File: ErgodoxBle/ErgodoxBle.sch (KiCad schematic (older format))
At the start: 93 parts, among them SW0:10 SW0:3, SW0:11 SW0:2, SW0:12 SW0:1, SW0:7 SW0:6, SW0:8 SW0:5, SW0:9 SW0:4, SW1:10 SW1:3, SW1:11 SW1:2, SW1:12 SW1:1, SW1:13 SW1:0, SW1:9 SW1:4, SW2:10 SW2:3, SW2:11 SW2:2, SW2:12 SW2:1, SW2:13 SW2:0, SW2:7 SW2:6, SW2:8 SW2:5, SW2:9 SW2:4, SW3:10 SW3:3, SW3:11 SW3:2, SW3:12 SW3:1, SW3:13 SW3:0, SW3:8 SW3:5, SW3:9 SW3:4, SW4:10 SW4:3, SW4:11 SW4:2, SW4:12 SW4:1, SW4:13 SW4:0, SW4:7 SW4:6, SW4:8 SW4:5, SW4:9 SW4:4, SW5:10 SW5:3, SW5:11 SW5:2, SW5:12 SW5:1, SW5:13 SW5:0, SW5:7 SW5:6, SW5:8 SW5:5, SW5:9 SW5:4

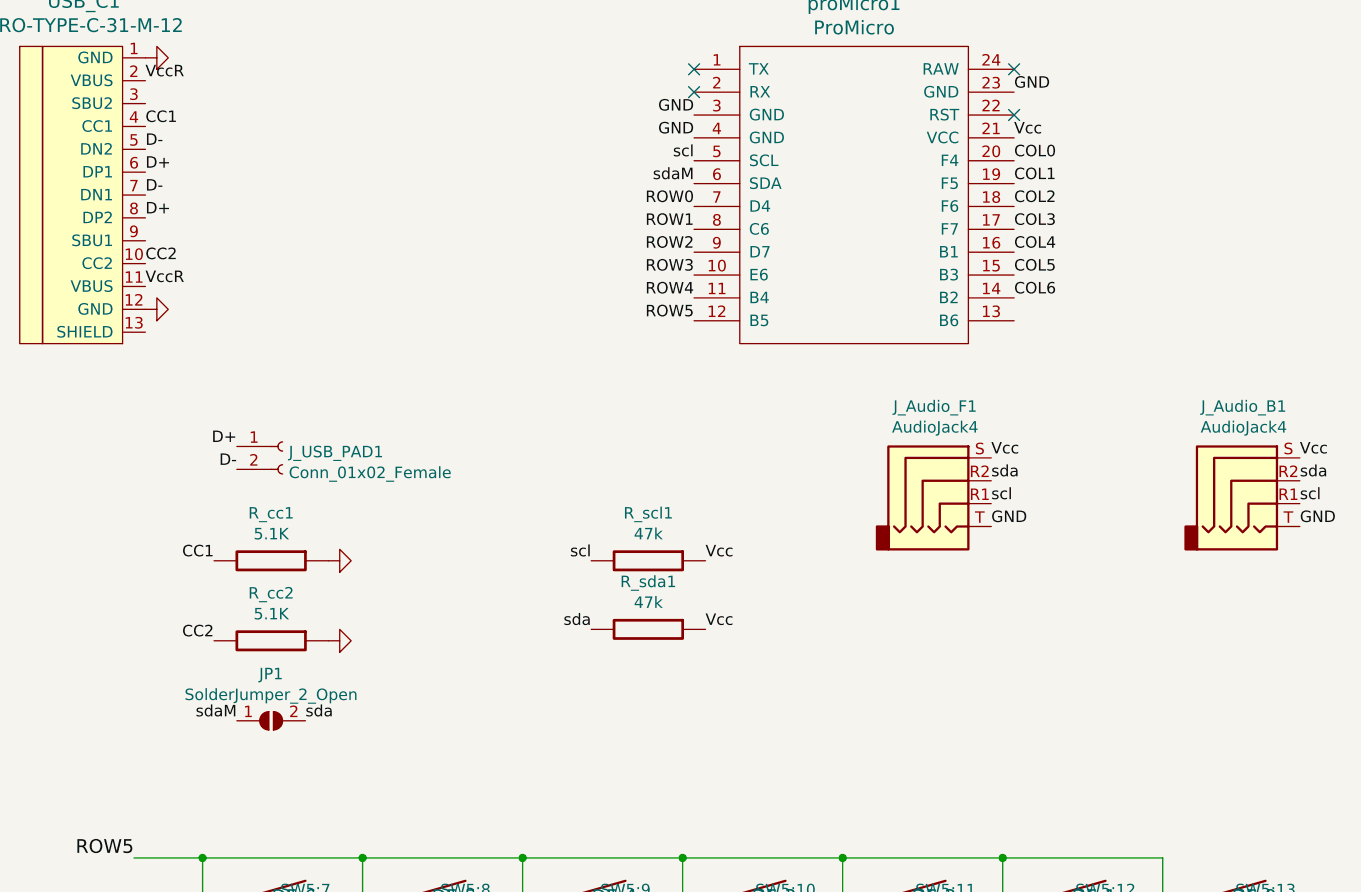
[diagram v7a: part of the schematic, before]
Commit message: update pcb, removed unwanted i2c wire, will go only serial over sda
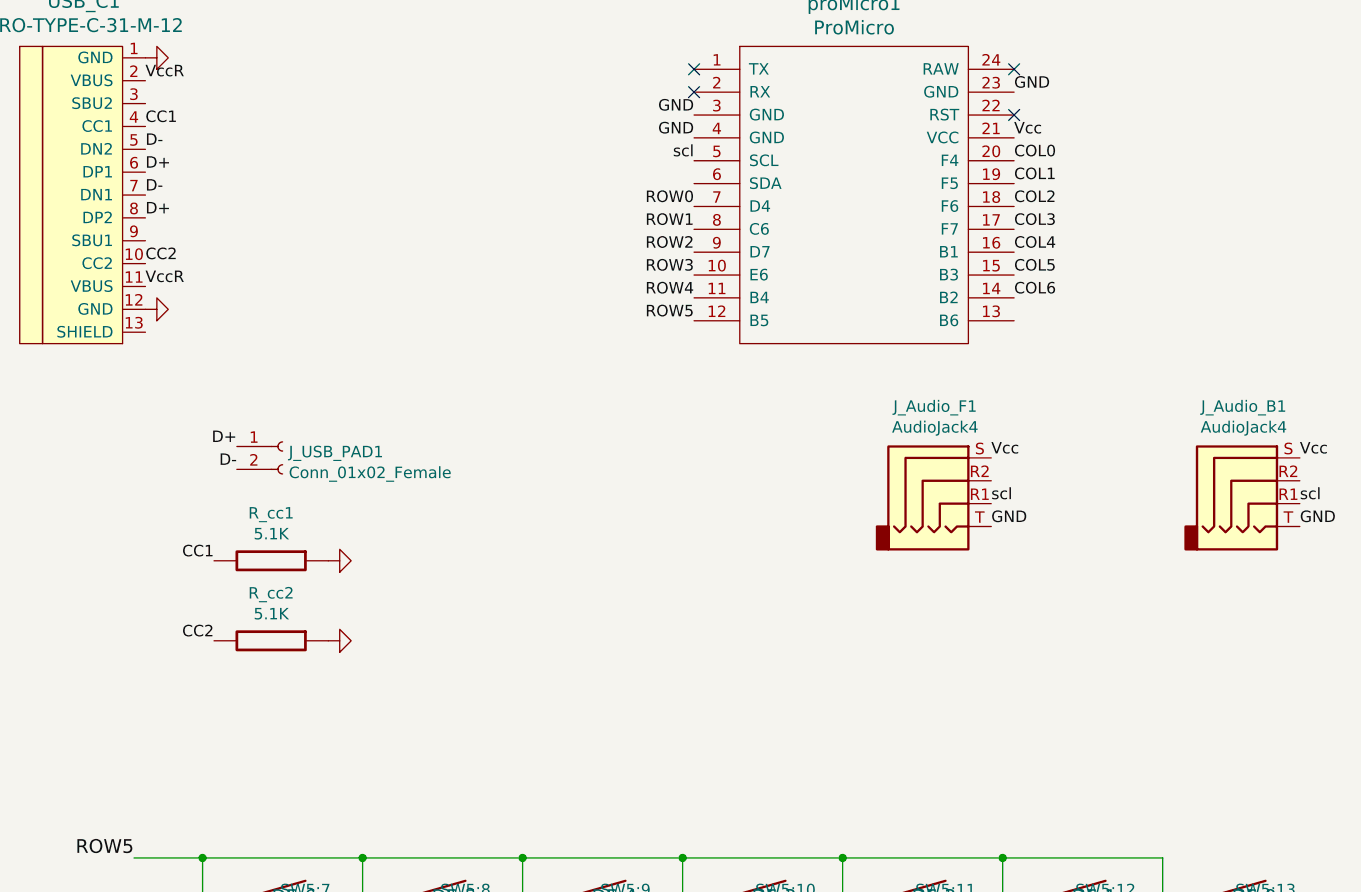
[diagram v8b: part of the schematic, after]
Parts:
- removed JP1: SolderJumper_2_Open, Keebio-Parts:solder_jumper, symbol Jumper:SolderJumper_2_Open
- removed R_scl1, R_sda1: 47k, Keebio-Parts:Resistor-Hybrid, symbol component:RESISTOR
- J_Audio_B1, J_Audio_F1: footprint Keebio-Parts:TRRS-PJ-320D -> Connector_Audio:Jack_3.5mm_PJ320D_Horizontal
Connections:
- net sda: no longer names the net of J_Audio_F1.R2
- net sda: no longer J_Audio_B1.R2
- net sdaM: no longer names the net of proMicro1.6 (SDA)
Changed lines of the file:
@@
 Text Label 3750 2750 2    50   ~ 0
 scl
-Text Label 3750 2850 2    50   ~ 0
-sdaM
 NoConn ~ 3750 2350
 NoConn ~ 3750 2450
 NoConn ~ 5150 2350
 NoConn ~ 5150 2550
-$Comp
-L Jumper:SolderJumper_2_Open JP1
-U 1 1 5C590F9B
-P 1900 5200
-F 0 "JP1" H 1900 5405 50  0000 C CNN
-F 1 "SolderJumper_2_Open" H 1900 5314 50  0000 C CNN
-F 2 "Keebio-Parts:solder_jumper" H 1900 5200 50  0001 C CNN
-F 3 "~" H 1900 5200 50  0001 C CNN
-	1    1900 5200
-	1    0    0    -1
-$EndComp
-Text Label 1750 5200 2    50   ~ 0
-sdaM
-Text Label 2050 5200 0    50   ~ 0
-sda
-$Comp
-L component:RESISTOR R_scl1
-U 1 1 5C5A4BE6
-P 3550 4500
-F 0 "R_scl1" V 3342 4500 50  0000 C CNN
-F 1 "47k" V 3433 4500 50  0000 C CNN
-F 2 "Keebio-Parts:Resistor-Hybrid" H 3550 4500 50  0001 C CNN
-F 3 "" H 3550 4500 50  0001 C CNN
-	1    3550 4500
-	0    1    1    0
-$EndComp
-$Comp
-L component:RESISTOR R_sda1
-U 1 1 5C5A4DA6
-P 3550 4800
-F 0 "R_sda1" V 3342 4800 50  0000 C CNN
-F 1 "47k" V 3433 4800 50  0000 C CNN
-F 2 "Keebio-Parts:Resistor-Hybrid" H 3550 4800 50  0001 C CNN
-F 3 "" H 3550 4800 50  0001 C CNN
-	1    3550 4800
-	0    1    1    0
-$EndComp
-Text Label 3800 4500 0    50   ~ 0
-Vcc
-Text Label 3800 4800 0    50   ~ 0
-Vcc
-Text Label 3300 4800 2    50   ~ 0
-sda
-Text Label 3300 4500 2    50   ~ 0
-scl
 $Comp
 L Connector:AudioJack4 J_Audio_F1
@@
 F 0 "J_Audio_F1" H 4805 4475 50  0000 C CNN
 F 1 "AudioJack4" H 4805 4384 50  0000 C CNN
-F 2 "Keebio-Parts:TRRS-PJ-320D" H 4850 4150 50  0001 C CNN
+F 2 "Connector_Audio:Jack_3.5mm_PJ320D_Horizontal" H 4850 4150 50  0001 C CNN
 F 3 "~" H 4850 4150 50  0001 C CNN
 	1    4850 4150
@@
 F 0 "J_Audio_B1" H 6155 4475 50  0000 C CNN
 F 1 "AudioJack4" H 6155 4384 50  0000 C CNN
-F 2 "Keebio-Parts:TRRS-PJ-320D" H 6200 4150 50  0001 C CNN
+F 2 "Connector_Audio:Jack_3.5mm_PJ320D_Horizontal" H 6200 4150 50  0001 C CNN
 F 3 "~" H 6200 4150 50  0001 C CNN
 	1    6200 4150
@@
 Text Label 5050 4350 0    50   ~ 0
 GND
-Text Label 5050 4150 0    50   ~ 0
-sda
 Text Label 5050 4250 0    50   ~ 0
 scl
 Text Label 6400 4050 0    50   ~ 0
 Vcc
-Text Label 6400 4150 0    50   ~ 0
-sda
 Text Label 6400 4250 0    50   ~ 0
 scl
